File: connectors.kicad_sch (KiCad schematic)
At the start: 3 parts, among them J4 JST_VH_B2P_3.96mm, J5 JST_VH_B2P_3.96mm, J6 JST_VH_B3P_3.96mm

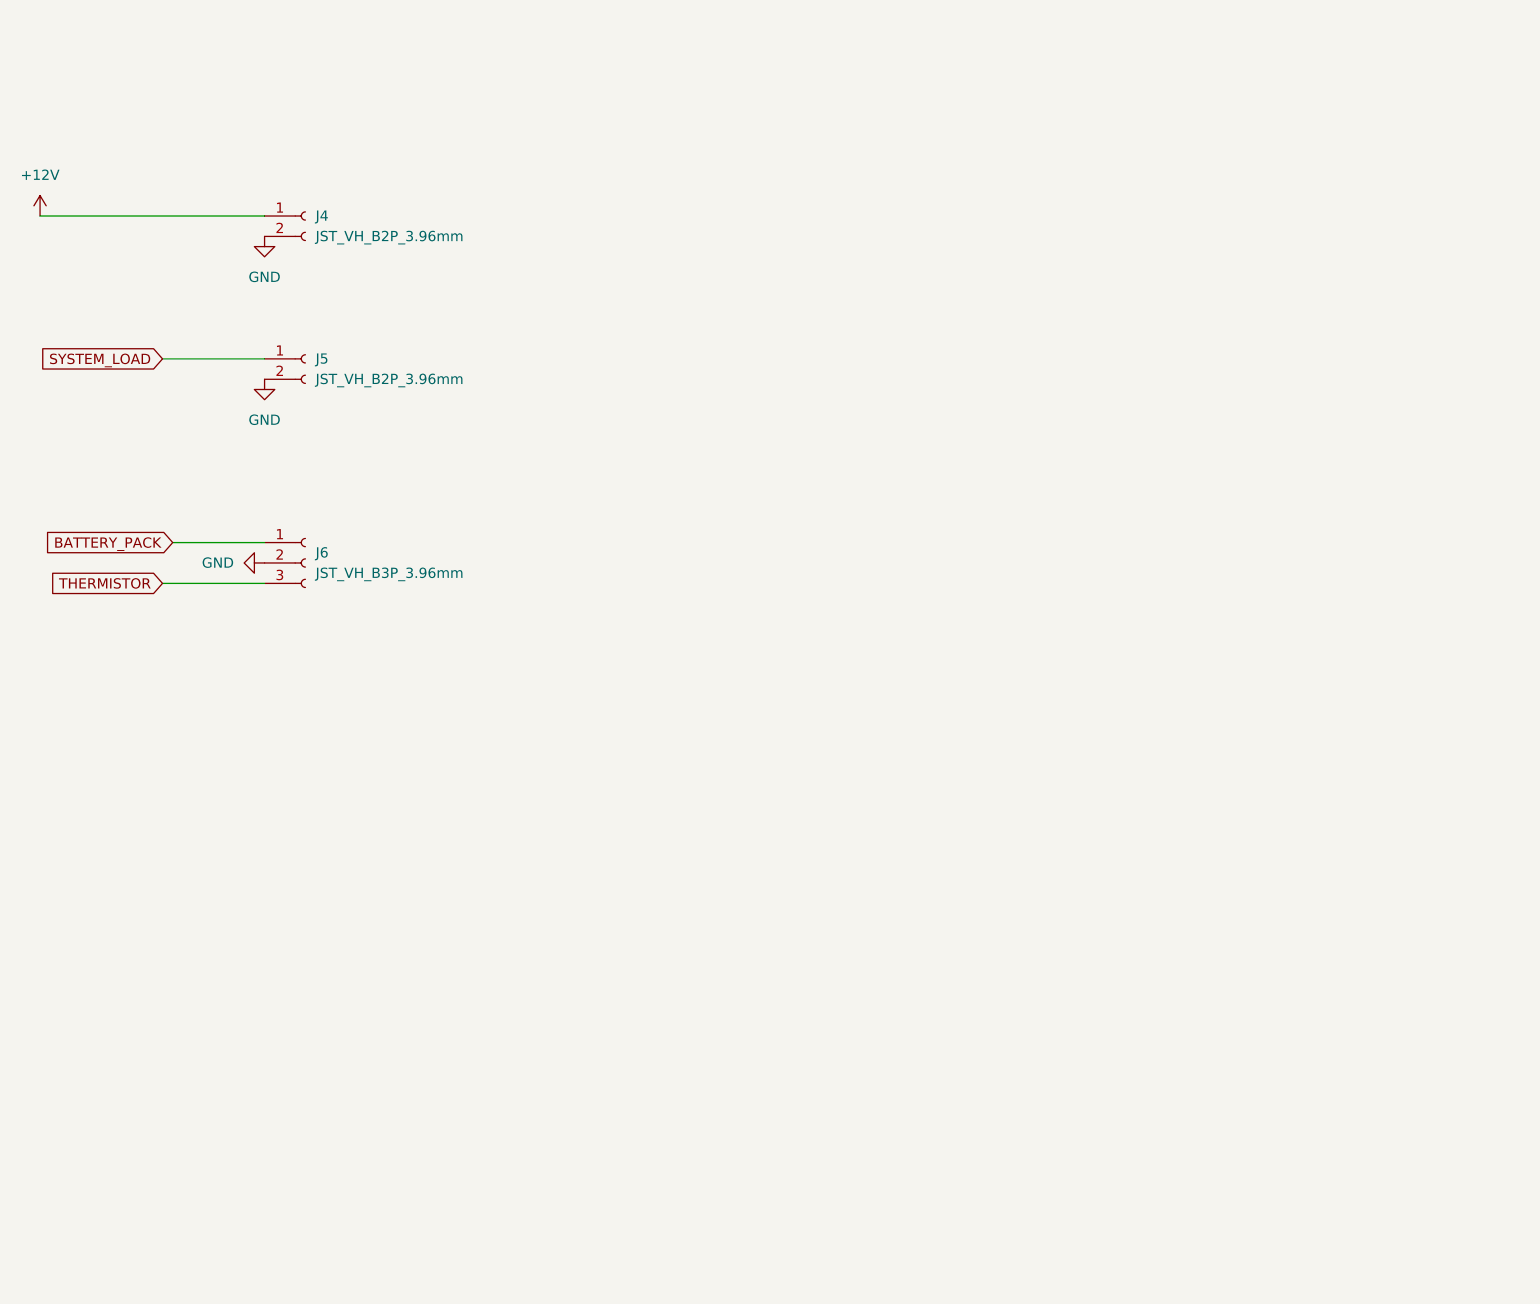
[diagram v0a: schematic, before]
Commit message: Change schematic sheet size to A4
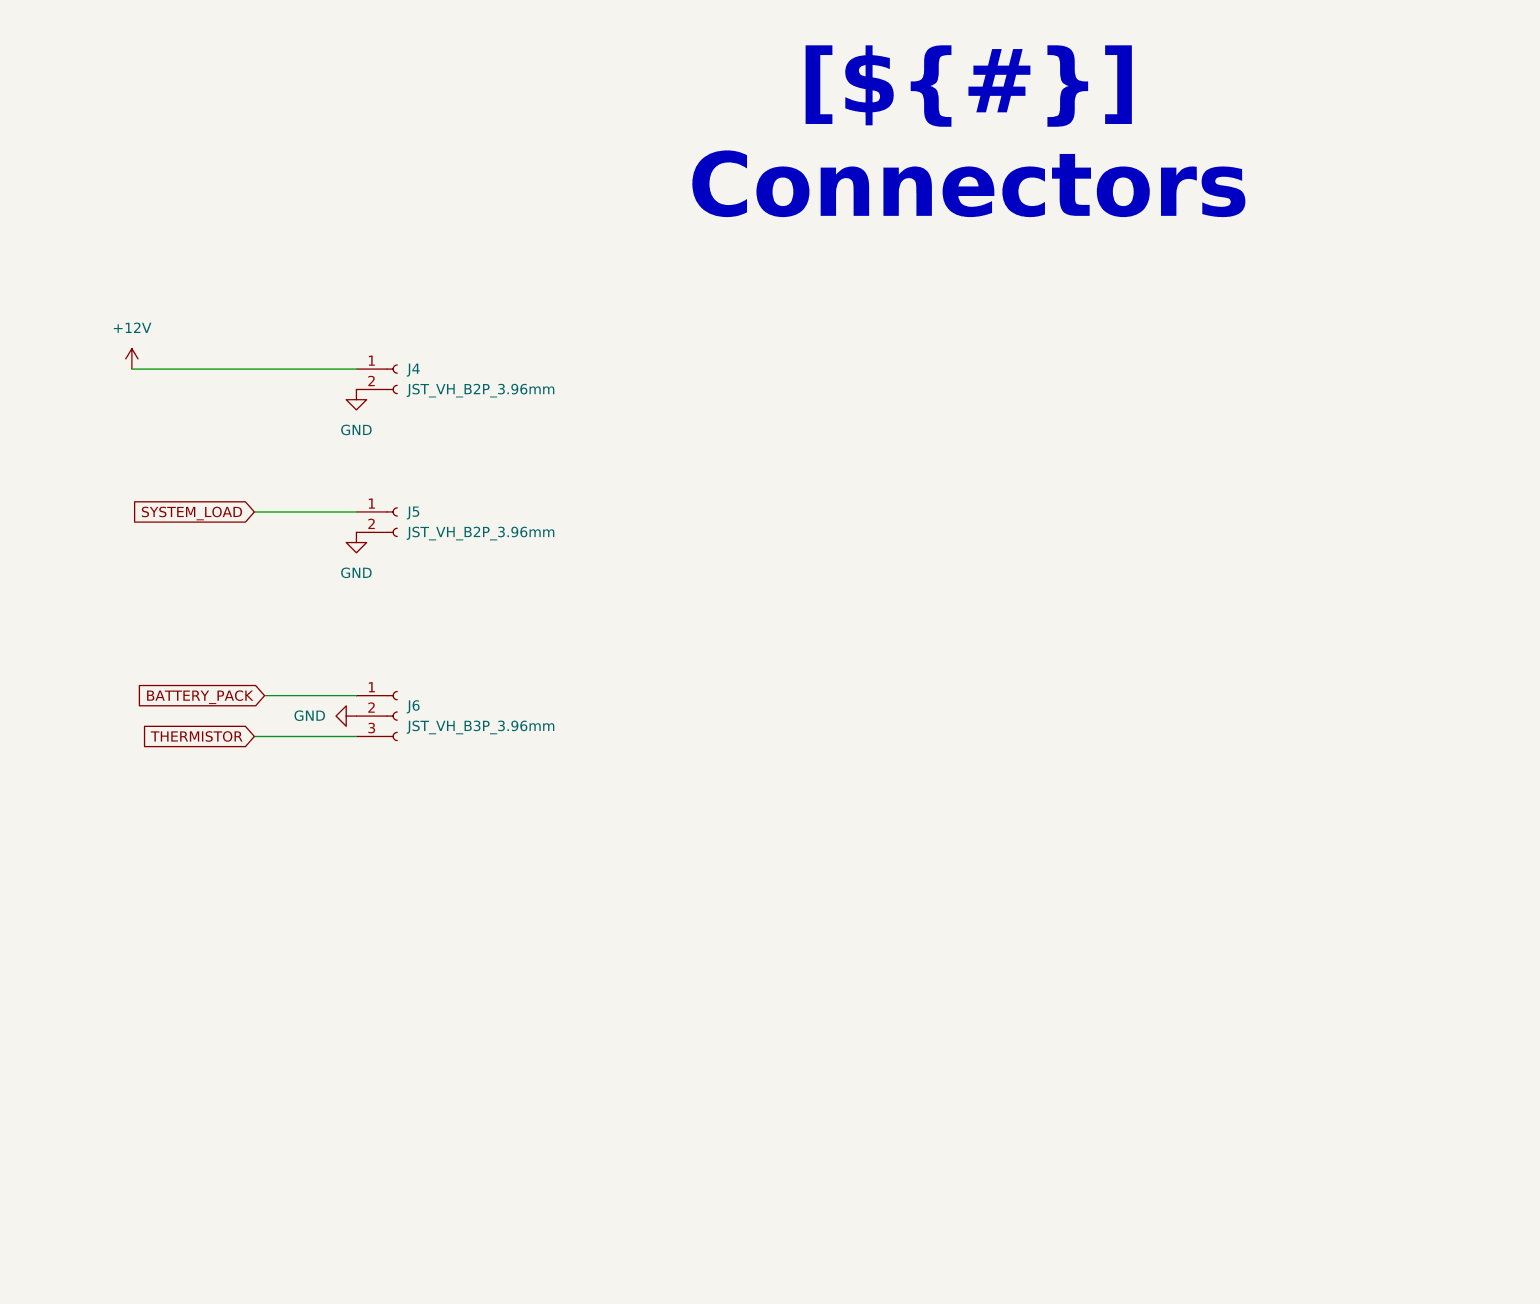
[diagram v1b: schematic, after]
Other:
- moved on the sheet: J4, J5, J6
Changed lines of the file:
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@@
 	(generator "eeschema")
 	(generator_version "9.0")
-	(paper "A3")
+	(paper "A4")
 	(title_block
 		(title "Connectors")
@@
 		(company "${COMPANY}")
 	)
+	(text_box "[${#}] ${TITLE}"
+		(exclude_from_sim no)
+		(at 97.79 16.51 0)
+		(size 96.52 12.7)
+		(margins 5.9999 5.9999 5.9999 5.9999)
+		(stroke
+			(width -0.0001)
+			(type default)
+		)
+		(fill
+			(type none)
+		)
+		(effects
+			(font
+				(face "Times New Roman")
+				(size 8 8)
+				(thickness 1.2)
+				(bold yes)
+				(color 162 22 34 1)
+			)
+		)
+	)
 	(wire
 		(pts
-			(xy 30.48 33.02) (xy 58.42 33.02)
+			(xy 41.91 52.07) (xy 69.85 52.07)
 		)
 		(stroke
@@
 	(wire
 		(pts
-			(xy 45.72 50.8) (xy 58.42 50.8)
+			(xy 57.15 69.85) (xy 69.85 69.85)
 		)
 		(stroke
@@
 	(wire
 		(pts
-			(xy 58.42 78.74) (xy 45.72 78.74)
+			(xy 69.85 97.79) (xy 57.15 97.79)
 		)
 		(stroke
@@
 	(wire
 		(pts
-			(xy 58.42 73.66) (xy 46.99 73.66)
+			(xy 69.85 92.71) (xy 58.42 92.71)
 		)
 		(stroke
@@
 	(global_label "BATTERY_PACK"
 		(shape input)
-		(at 46.99 73.66 180)
+		(at 58.42 92.71 180)
 		(fields_autoplaced yes)
 		(effects
@@
 		)
 		(property "Intersheetrefs" "${INTERSHEET_REFS}"
-			(at 30.3372 73.66 0)
+			(at 41.7672 92.71 0)
 			(effects
 				(font
@@
 	(global_label "SYSTEM_LOAD"
 		(shape input)
-		(at 45.72 50.8 180)
+		(at 57.15 69.85 180)
 		(fields_autoplaced yes)
 		(effects
@@
 		)
 		(property "Intersheetrefs" "${INTERSHEET_REFS}"
-			(at 29.9744 50.8 0)
+			(at 41.4044 69.85 0)
 			(effects
 				(font
@@
 	(global_label "THERMISTOR"
 		(shape input)
-		(at 45.72 78.74 180)
+		(at 57.15 97.79 180)
 		(fields_autoplaced yes)
 		(effects
@@
 		)
 		(property "Intersheetrefs" "${INTERSHEET_REFS}"
-			(at 31.1839 78.74 0)
+			(at 42.6139 97.79 0)
 			(effects
 				(font
@@
 	(symbol
 		(lib_id "Connector:Conn_01x02_Socket")
-		(at 63.5 50.8 0)
+		(at 74.93 69.85 0)
 		(unit 1)
 		(exclude_from_sim no)
@@
 		(fields_autoplaced yes)
 		(property "Reference" "J5"
-			(at 64.77 50.7999 0)
+			(at 76.2 69.8499 0)
 			(effects
 				(font
@@
 		)
 		(property "Value" "JST_VH_B2P_3.96mm"
-			(at 64.77 53.3399 0)
+			(at 76.2 72.3899 0)
 			(effects
 				(font
@@
 		)
 		(property "Footprint" "Connector_JST:JST_VH_B2P-VH_1x02_P3.96mm_Vertical"
-			(at 63.5 50.8 0)
+			(at 74.93 69.85 0)
 			(effects
 				(font
@@
 		)
 		(property "Datasheet" "~"
-			(at 63.5 50.8 0)
+			(at 74.93 69.85 0)
 			(effects
 				(font
@@
 		)
 		(property "Description" "Generic connector, single row, 01x02, script generated"
-			(at 63.5 50.8 0)
+			(at 74.93 69.85 0)
 			(effects
 				(font
@@
 	(symbol
 		(lib_id "power:GND")
-		(at 58.42 76.2 270)
+		(at 69.85 95.25 270)
 		(unit 1)
 		(exclude_from_sim no)
@@
 		(fields_autoplaced yes)
 		(property "Reference" "#PWR032"
-			(at 52.07 76.2 0)
+			(at 63.5 95.25 0)
 			(effects
 				(font
@@
 		)
 		(property "Value" "GND"
-			(at 54.61 76.1999 90)
+			(at 66.04 95.2499 90)
 			(effects
 				(font
@@
 		)
 		(property "Footprint" ""
-			(at 58.42 76.2 0)
+			(at 69.85 95.25 0)
 			(effects
 				(font
@@
 		)
 		(property "Datasheet" ""
-			(at 58.42 76.2 0)
+			(at 69.85 95.25 0)
 			(effects
 				(font
@@
 		)
 		(property "Description" "Power symbol creates a global label with name \"GND\" , ground"
-			(at 58.42 76.2 0)
+			(at 69.85 95.25 0)
 			(effects
 				(font
@@
 	(symbol
 		(lib_id "power:GND")
-		(at 58.42 53.34 0)
+		(at 69.85 72.39 0)
 		(unit 1)
 		(exclude_from_sim no)
@@
 		(fields_autoplaced yes)
 		(property "Reference" "#PWR031"
-			(at 58.42 59.69 0)
+			(at 69.85 78.74 0)
 			(effects
 				(font
@@
 		)
 		(property "Value" "GND"
-			(at 58.42 58.42 0)
+			(at 69.85 77.47 0)
 			(effects
 				(font
@@
 		)
 		(property "Footprint" ""
-			(at 58.42 53.34 0)
+			(at 69.85 72.39 0)
 			(effects
 				(font
@@
 		)
 		(property "Datasheet" ""
-			(at 58.42 53.34 0)
+			(at 69.85 72.39 0)
 			(effects
 				(font
@@
 		)
 		(property "Description" "Power symbol creates a global label with name \"GND\" , ground"
-			(at 58.42 53.34 0)
+			(at 69.85 72.39 0)
 			(effects
 				(font
@@
 	(symbol
 		(lib_id "power:GND")
-		(at 58.42 35.56 0)
+		(at 69.85 54.61 0)
 		(unit 1)
 		(exclude_from_sim no)
@@
 		(fields_autoplaced yes)
 		(property "Reference" "#PWR030"
-			(at 58.42 41.91 0)
+			(at 69.85 60.96 0)
 			(effects
 				(font
@@
 		)
 		(property "Value" "GND"
-			(at 58.42 40.64 0)
+			(at 69.85 59.69 0)
 			(effects
 				(font
@@
 		)
 		(property "Footprint" ""
-			(at 58.42 35.56 0)
+			(at 69.85 54.61 0)
 			(effects
 				(font
@@
 		)
 		(property "Datasheet" ""
-			(at 58.42 35.56 0)
+			(at 69.85 54.61 0)
 			(effects
 				(font
@@
 		)
 		(property "Description" "Power symbol creates a global label with name \"GND\" , ground"
-			(at 58.42 35.56 0)
+			(at 69.85 54.61 0)
 			(effects
 				(font
@@
 	(symbol
 		(lib_id "power:+12V")
-		(at 30.48 33.02 0)
+		(at 41.91 52.07 0)
 		(unit 1)
 		(exclude_from_sim no)
@@
 		(fields_autoplaced yes)
 		(property "Reference" "#PWR029"
-			(at 30.48 36.83 0)
+			(at 41.91 55.88 0)
 			(effects
 				(font
@@
 		)
 		(property "Value" "+12V"
-			(at 30.48 27.94 0)
+			(at 41.91 46.99 0)
 			(effects
 				(font
@@
 		)
 		(property "Footprint" ""
-			(at 30.48 33.02 0)
+			(at 41.91 52.07 0)
 			(effects
 				(font
@@
 		)
 		(property "Datasheet" ""
-			(at 30.48 33.02 0)
+			(at 41.91 52.07 0)
 			(effects
 				(font
@@
 		)
 		(property "Description" "Power symbol creates a global label with name \"+12V\""
-			(at 30.48 33.02 0)
+			(at 41.91 52.07 0)
 			(effects
 				(font
@@
 	(symbol
 		(lib_id "Connector:Conn_01x02_Socket")
-		(at 63.5 33.02 0)
+		(at 74.93 52.07 0)
 		(unit 1)
 		(exclude_from_sim no)
@@
 		(fields_autoplaced yes)
 		(property "Reference" "J4"
-			(at 64.77 33.0199 0)
+			(at 76.2 52.0699 0)
 			(effects
 				(font
@@
 		)
 		(property "Value" "JST_VH_B2P_3.96mm"
-			(at 64.77 35.5599 0)
+			(at 76.2 54.6099 0)
 			(effects
 				(font
@@
 		)
 		(property "Footprint" "Connector_JST:JST_VH_B2P-VH_1x02_P3.96mm_Vertical"
-			(at 63.5 33.02 0)
+			(at 74.93 52.07 0)
 			(effects
 				(font
@@
 		)
 		(property "Datasheet" "~"
-			(at 63.5 33.02 0)
+			(at 74.93 52.07 0)
 			(effects
 				(font
@@
 		)
 		(property "Description" "Generic connector, single row, 01x02, script generated"
-			(at 63.5 33.02 0)
+			(at 74.93 52.07 0)
 			(effects
 				(font
@@
 	(symbol
 		(lib_id "Connector:Conn_01x03_Socket")
-		(at 63.5 76.2 0)
+		(at 74.93 95.25 0)
 		(unit 1)
 		(exclude_from_sim no)
@@
 		(fields_autoplaced yes)
 		(property "Reference" "J6"
-			(at 64.77 74.9299 0)
+			(at 76.2 93.9799 0)
 			(effects
 				(font
@@
 		)
 		(property "Value" "JST_VH_B3P_3.96mm"
-			(at 64.77 77.4699 0)
+			(at 76.2 96.5199 0)
 			(effects
 				(font
@@
 		)
 		(property "Footprint" "Connector_JST:JST_VH_B3P-VH_1x03_P3.96mm_Vertical"
-			(at 63.5 76.2 0)
+			(at 74.93 95.25 0)
 			(effects
 				(font
@@
 		)
 		(property "Datasheet" "~"
-			(at 63.5 76.2 0)
+			(at 74.93 95.25 0)
 			(effects
 				(font
@@
 		)
 		(property "Description" "Generic connector, single row, 01x03, script generated"
-			(at 63.5 76.2 0)
-			(effects
-				(font
+			(at 74.93 95.25 0)
+			(effects
+				(font

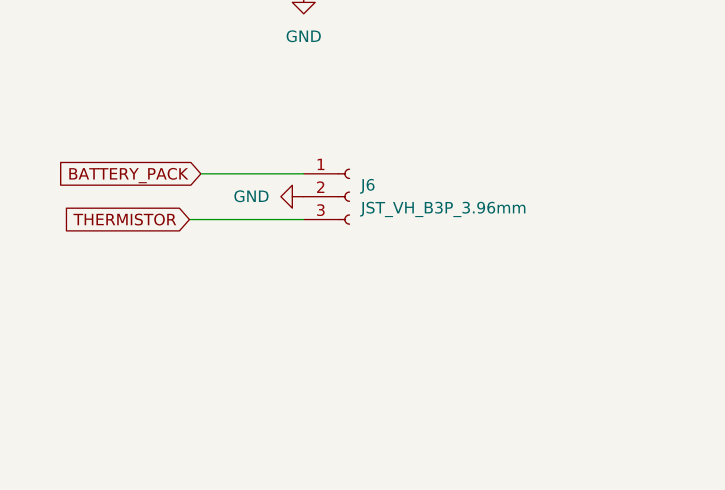
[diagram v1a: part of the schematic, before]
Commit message: Add cell balancer - in progress
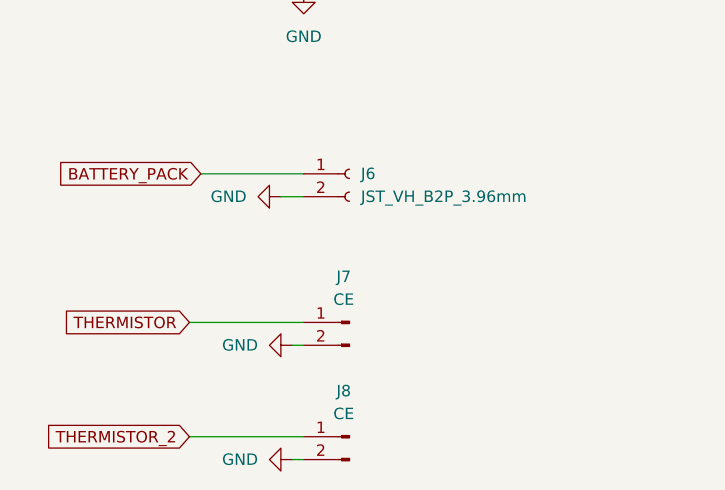
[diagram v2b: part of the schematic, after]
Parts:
- removed J6: JST_VH_B3P_3.96mm, Connector_JST:JST_VH_B3P-VH_1x03_P3.96mm_Vertical, symbol Connector:Conn_01x03_Socket
- added J6: JST_VH_B2P_3.96mm, Connector_JST:JST_VH_B2P-VH_1x02_P3.96mm_Vertical, symbol Connector:Conn_01x02_Socket
- added J7, J8: CE, Connector_PinHeader_2.54mm:PinHeader_1x02_P2.54mm_Vertical, symbol Connector:Conn_01x02_Pin
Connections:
- net BATTERY_PACK: now also J6.1 (Pin_1)
- net GND: now also J6.2 (Pin_2), J7.2 (Pin_2), J8.2 (Pin_2)
- net THERMISTOR: now also J7.1 (Pin_1)
- new net THERMISTOR_2: J8.1 (Pin_1)

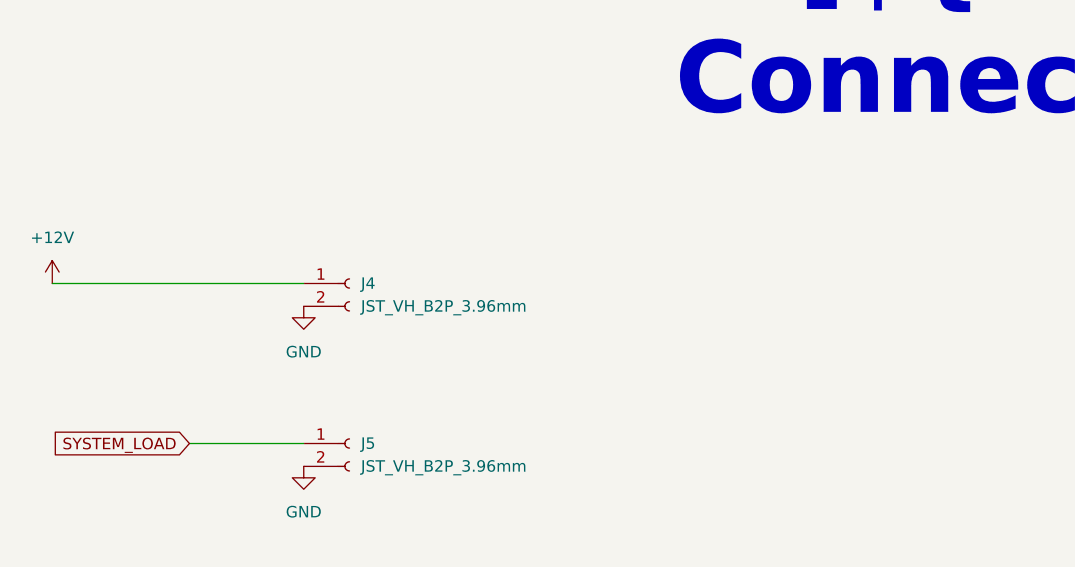
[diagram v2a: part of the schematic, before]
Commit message: Finish schematic
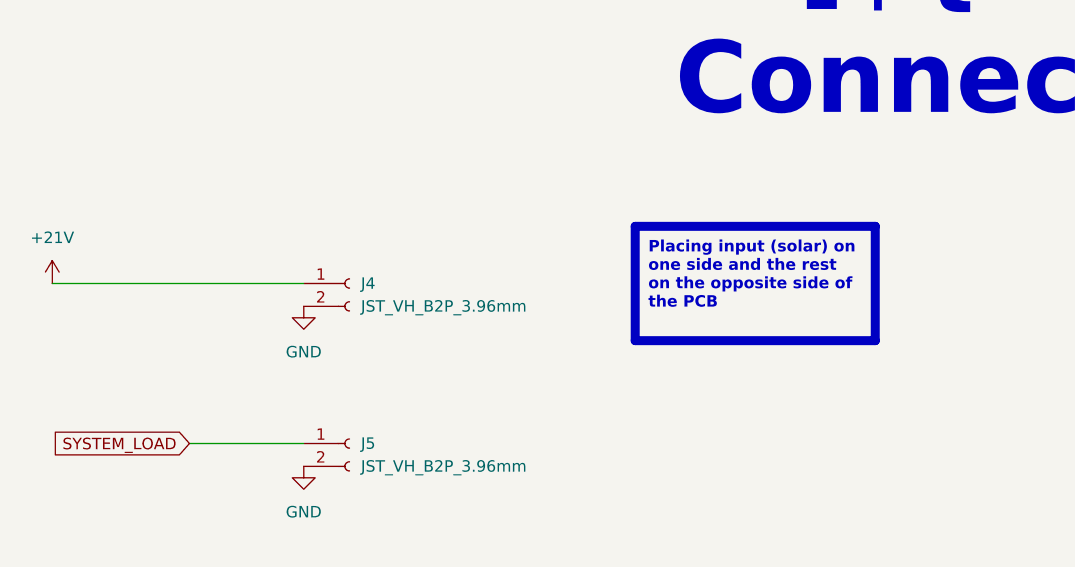
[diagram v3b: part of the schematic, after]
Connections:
- net +12V renamed +21V
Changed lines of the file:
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@@
 		(company "${COMPANY}")
+	)
+	(text_box "Placing input (solar) on one side and the rest on the opposite side of the PCB"
+		(exclude_from_sim no)
+		(at 106.68 45.72 0)
+		(size 26.67 12.7)
+		(margins 1.4525 1.4525 1.4525 1.4525)
+		(stroke
+			(width 1)
+			(type solid)
+			(color 0 0 255 1)
+		)
+		(fill
+			(type none)
+		)
+		(effects
+			(font
+				(face "Arial")
+				(size 1.27 1.27)
+				(thickness 0.4)
+				(bold yes)
+				(color 0 0 255 1)
+			)
+			(justify left top)
+		)
 	)
 	(text_box "[${#}] ${TITLE}"
@@
 			)
 		)
-		(property "Description" "Generic connector, single row, 01x02, script generated"
+		(property "Description" "JST_VH_B2P_3.96mm"
 			(at 74.93 69.85 0)
 			(effects
@@
 		(dnp no)
 		(fields_autoplaced yes)
-		(property "Reference" "#PWR032"
+		(property "Reference" "#PWR040"
 			(at 60.96 95.25 0)
 			(effects
@@
 			(project "solar_smart_station"
 				(path "/f9e05184-c88b-4a88-ae9c-ab2bdb32be7c/c5103ceb-5325-4a84-a025-9638a412984e/ae8d0caf-6898-4dee-88e6-fcc8a5387577"
-					(reference "#PWR032")
+					(reference "#PWR040")
 					(unit 1)
 				)
@@
 		(dnp no)
 		(fields_autoplaced yes)
-		(property "Reference" "#PWR031"
+		(property "Reference" "#PWR044"
 			(at 69.85 78.74 0)
 			(effects
@@
 			(project "solar_smart_station"
 				(path "/f9e05184-c88b-4a88-ae9c-ab2bdb32be7c/c5103ceb-5325-4a84-a025-9638a412984e/ae8d0caf-6898-4dee-88e6-fcc8a5387577"
-					(reference "#PWR031")
+					(reference "#PWR044")
 					(unit 1)
 				)
@@
 		(dnp no)
 		(fields_autoplaced yes)
-		(property "Reference" "#PWR030"
+		(property "Reference" "#PWR043"
 			(at 69.85 60.96 0)
 			(effects
@@
 			(project "solar_smart_station"
 				(path "/f9e05184-c88b-4a88-ae9c-ab2bdb32be7c/c5103ceb-5325-4a84-a025-9638a412984e/ae8d0caf-6898-4dee-88e6-fcc8a5387577"
-					(reference "#PWR030")
+					(reference "#PWR043")
 					(unit 1)
 				)
@@
 			)
 		)
-		(property "Description" "Generic connector, single row, 01x02, script generated"
+		(property "Description" "JST_VH_B2P_3.96mm"
 			(at 74.93 92.71 0)
 			(effects
@@
 		(dnp no)
 		(fields_autoplaced yes)
-		(property "Reference" "#PWR029"
+		(property "Reference" "#PWR039"
 			(at 41.91 55.88 0)
 			(effects
@@
 			)
 		)
-		(property "Value" "+12V"
+		(property "Value" "+21V"
 			(at 41.91 46.99 0)
 			(effects
@@
 			(project "solar_smart_station"
 				(path "/f9e05184-c88b-4a88-ae9c-ab2bdb32be7c/c5103ceb-5325-4a84-a025-9638a412984e/ae8d0caf-6898-4dee-88e6-fcc8a5387577"
-					(reference "#PWR029")
+					(reference "#PWR039")
 					(unit 1)
 				)
@@
 			)
 		)
-		(property "Description" "Generic connector, single row, 01x02, script generated"
+		(property "Description" "JST_VH_B2P_3.96mm"
 			(at 74.93 52.07 0)
 			(effects
